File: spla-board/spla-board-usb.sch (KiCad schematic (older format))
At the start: 28 parts, among them J1 USB_B_Micro, U2 FT2232H, U3 93LC66B, X1 FT5HNBPK12.0-T1

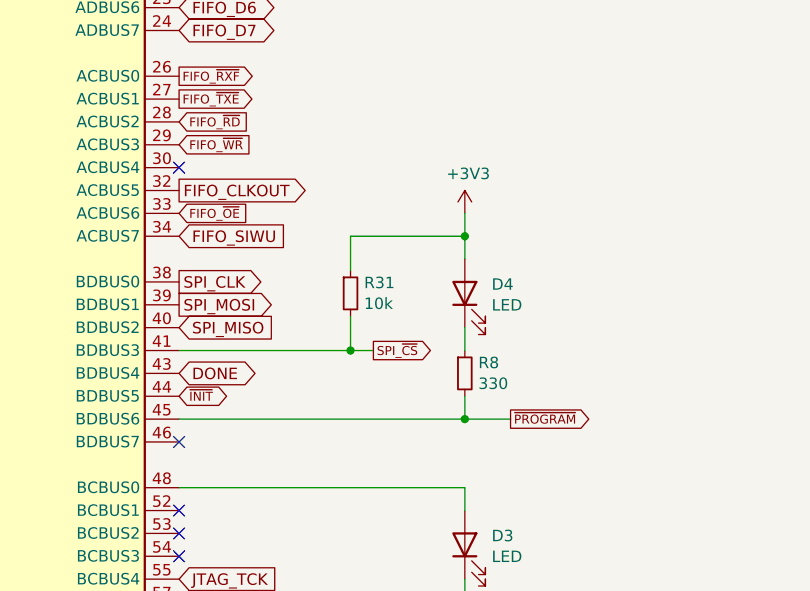
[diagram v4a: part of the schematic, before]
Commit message: schematic/pcb: Pinswap entire FPGA to put LEDs/TPs on south edge.
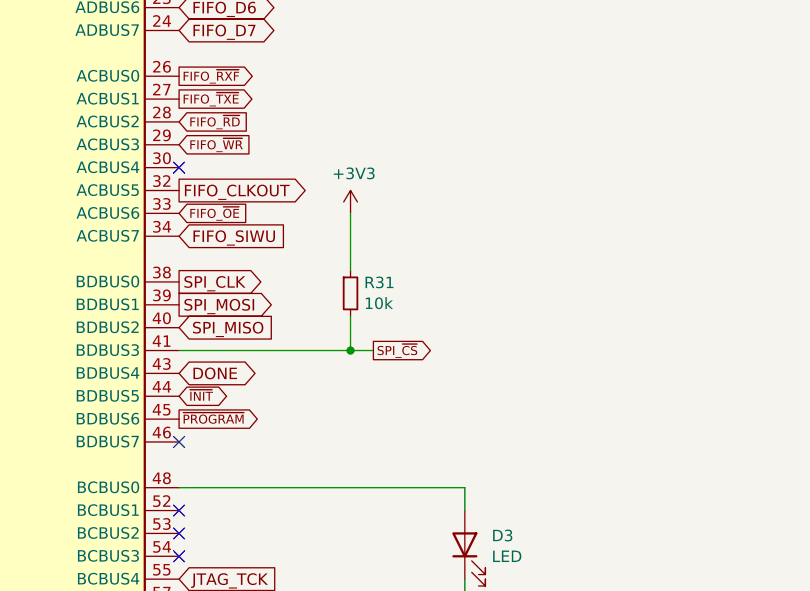
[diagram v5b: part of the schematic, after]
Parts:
- removed D4: LED, LED_SMD:LED_0805_2012Metric, symbol Device:LED
- removed R8: 330, Resistor_SMD:R_0603_1608Metric, symbol Device:R_Small
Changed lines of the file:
@@
 Text GLabel 11150 6050 2    39   BiDi ~ 0
 ~INIT
-Text GLabel 12600 6150 2    39   Output ~ 0
+Text GLabel 11150 6150 2    39   Output ~ 0
 ~PROGRAM
 Text GLabel 11150 5950 2    50   BiDi ~ 0
@@
 $EndComp
 $Comp
-L Device:LED D4
-U 1 1 5E9C89B2
-P 12400 5600
-AR Path="/5E4F712F/5E9C89B2" Ref="D4"  Part="1"
-AR Path="/5E50D39B/5E9C89B2" Ref="D?"  Part="1"
-AR Path="/5E4D8358/5E9C89B2" Ref="D?"  Part="1"
-F 0 "D4" V 12439 5483 50  0000 R CNN
-F 1 "LED" V 12348 5483 50  0000 R CNN
-F 2 "LED_SMD:LED_0805_2012Metric" H 12400 5600 50  0001 C CNN
-F 3 "~" H 12400 5600 50  0001 C CNN
-F 4 "732-4986-1-ND" H 12400 5600 50  0001 C CNN "Digikey"
-F 5 "150080VS75000" H 12400 5600 50  0001 C CNN "Manufacturer Id"
-F 6 "Wuerth Electronik" H 12400 5600 50  0001 C CNN "Manufacturer"
-	1    12400 5600
-	0    -1   -1   0
-$EndComp
-Wire Wire Line
-	12400 5750 12400 5850
-Wire Wire Line
-	12400 6050 12400 6150
-$Comp
 L power:+3V3 #PWR?
 U 1 1 5E9C89C1
-P 12400 5250
+P 11900 5250
 AR Path="/5E4D8358/5E9C89C1" Ref="#PWR?"  Part="1"
 AR Path="/5E4F712F/5E9C89C1" Ref="#PWR053"  Part="1"
-F 0 "#PWR053" H 12400 5100 50  0001 C CNN
-F 1 "+3V3" H 12415 5423 50  0000 C CNN
-F 2 "" H 12400 5250 50  0001 C CNN
-F 3 "" H 12400 5250 50  0001 C CNN
-	1    12400 5250
-	1    0    0    -1
-$EndComp
-Wire Wire Line
-	12400 5250 12400 5350
-Wire Wire Line
-	12600 6150 12400 6150
-Connection ~ 12400 6150
-Wire Wire Line
-	12400 6150 11150 6150
+F 0 "#PWR053" H 11900 5100 50  0001 C CNN
+F 1 "+3V3" H 11915 5423 50  0000 C CNN
+F 2 "" H 11900 5250 50  0001 C CNN
+F 3 "" H 11900 5250 50  0001 C CNN
+	1    11900 5250
+	1    0    0    -1
+$EndComp
 Wire Wire Line
 	6350 7450 7550 7450
@@
 $EndComp
 Wire Wire Line
-	12400 5350 11900 5350
-Wire Wire Line
-	11900 5350 11900 5500
-Connection ~ 12400 5350
-Wire Wire Line
-	12400 5350 12400 5450
-Wire Wire Line
 	2800 4450 2800 4200
 Wire Wire Line
@@
 F 6 "GRM188R61E475KE11D" H 7300 2900 50  0001 C CNN "Manufacturer Id"
 	1    7300 2900
-	1    0    0    -1
-$EndComp
-$Comp
-L Device:R_Small R8
-U 1 1 5E9C89B8
-P 12400 5950
-AR Path="/5E4F712F/5E9C89B8" Ref="R8"  Part="1"
-AR Path="/5E50D39B/5E9C89B8" Ref="R?"  Part="1"
-AR Path="/5E4D8358/5E9C89B8" Ref="R?"  Part="1"
-F 0 "R8" H 12459 5996 50  0000 L CNN
-F 1 "330" H 12459 5905 50  0000 L CNN
-F 2 "Resistor_SMD:R_0603_1608Metric" H 12400 5950 50  0001 C CNN
-F 3 "~" H 12400 5950 50  0001 C CNN
-F 4 "RMCF0603JT330RCT-ND" H 12400 5950 50  0001 C CNN "Digikey"
-F 5 "Stackpole Electronics Inc" H 12400 5950 50  0001 C CNN "Manufacturer"
-F 6 "RMCF0603JT330R" H 12400 5950 50  0001 C CNN "Manufacturer Id"
-	1    12400 5950
 	1    0    0    -1
 $EndComp
@@
 Wire Wire Line
 	3950 3950 3950 4250
+Wire Wire Line
+	11900 5250 11900 5500
 $EndSCHEMATC

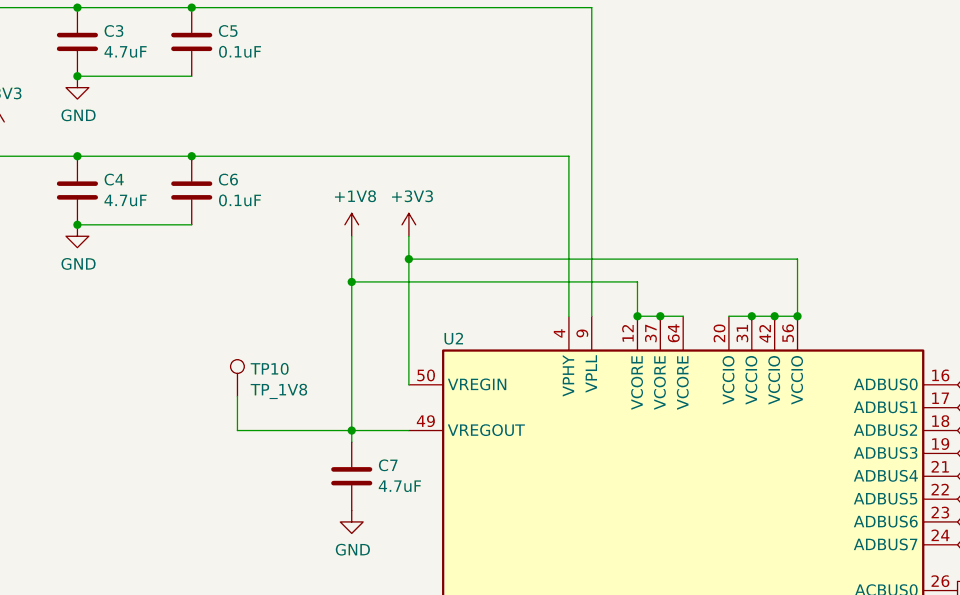
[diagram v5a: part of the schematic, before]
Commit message: schematic/pcb: Add 0-ohm resistor to disconnect FTDI 1.8V regulator.
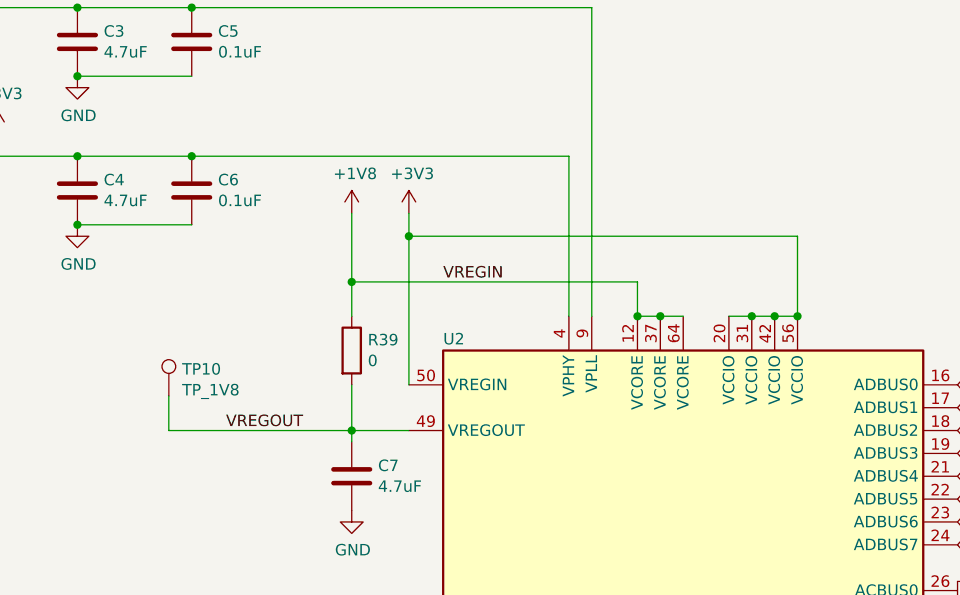
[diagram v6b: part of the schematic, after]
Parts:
- added R39: 0, Resistor_SMD:R_0603_1608Metric, symbol Device:R
- TP10: footprint TestPoint:TestPoint_Pad_D2.0mm -> TestPoint:TestPoint_Pad_D1.0mm
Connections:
- net +1V8: now also R39.1; no longer C7.1, TP10.1, U2.49 (VREGOUT)
- new net VREGOUT: C7.1, R39.2, TP10.1, U2.49 (VREGOUT)
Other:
- moved on the sheet: TP10
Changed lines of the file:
@@
 Weak pullup resistors
 Wire Wire Line
-	10450 3200 10450 3450
+	10450 3100 10450 3450
 Wire Wire Line
 	10150 3450 10250 3450
@@
 Wire Wire Line
 	10350 3450 10450 3450
-Wire Wire Line
-	8500 3300 8500 3950
 Wire Wire Line
 	8500 3950 8750 3950
@@
 L power:+1V8 #PWR0107
 U 1 1 5E5F64FC
-P 8500 3100
-F 0 "#PWR0107" H 8500 2950 50  0001 C CNN
-F 1 "+1V8" H 8515 3273 50  0000 C CNN
-F 2 "" H 8500 3100 50  0001 C CNN
-F 3 "" H 8500 3100 50  0001 C CNN
-	1    8500 3100
-	1    0    0    -1
-$EndComp
-Wire Wire Line
-	8500 3100 8500 3300
-Connection ~ 8500 3300
+P 8500 3000
+F 0 "#PWR0107" H 8500 2850 50  0001 C CNN
+F 1 "+1V8" H 8515 3173 50  0000 C CNN
+F 2 "" H 8500 3000 50  0001 C CNN
+F 3 "" H 8500 3000 50  0001 C CNN
+	1    8500 3000
+	1    0    0    -1
+$EndComp
+Wire Wire Line
+	8500 3000 8500 3300
 $Comp
 L power:GND #PWR0108
@@
 $EndComp
 Wire Wire Line
-	8750 3200 10450 3200
-Wire Wire Line
-	8750 3200 8750 3750
+	8750 3100 10450 3100
+Wire Wire Line
+	8750 3100 8750 3750
 $Comp
 L power:+3V3 #PWR0113
 U 1 1 5E65F7B7
-P 8750 3100
-F 0 "#PWR0113" H 8750 2950 50  0001 C CNN
-F 1 "+3V3" H 8765 3273 50  0000 C CNN
-F 2 "" H 8750 3100 50  0001 C CNN
-F 3 "" H 8750 3100 50  0001 C CNN
-	1    8750 3100
-	1    0    0    -1
-$EndComp
-Connection ~ 8750 3200
-Wire Wire Line
-	8750 3200 8750 3100
+P 8750 3000
+F 0 "#PWR0113" H 8750 2850 50  0001 C CNN
+F 1 "+3V3" H 8765 3173 50  0000 C CNN
+F 2 "" H 8750 3000 50  0001 C CNN
+F 3 "" H 8750 3000 50  0001 C CNN
+	1    8750 3000
+	1    0    0    -1
+$EndComp
+Connection ~ 8750 3100
+Wire Wire Line
+	8750 3100 8750 3000
 Wire Wire Line
 	9450 3450 9450 2750
@@
 L Connector:TestPoint TP10
 U 1 1 5F33FE5B
-P 8000 3800
-F 0 "TP10" H 8058 3918 50  0000 L CNN
-F 1 "TP_1V8" H 8058 3827 50  0000 L CNN
-F 2 "TestPoint:TestPoint_Pad_D2.0mm" H 8200 3800 50  0001 C CNN
-F 3 "~" H 8200 3800 50  0001 C CNN
-	1    8000 3800
-	1    0    0    -1
-$EndComp
-Wire Wire Line
-	8500 3950 8000 3950
-Wire Wire Line
-	8000 3950 8000 3800
+P 7700 3800
+F 0 "TP10" H 7758 3918 50  0000 L CNN
+F 1 "TP_1V8" H 7758 3827 50  0000 L CNN
+F 2 "TestPoint:TestPoint_Pad_D1.0mm" H 7900 3800 50  0001 C CNN
+F 3 "~" H 7900 3800 50  0001 C CNN
+	1    7700 3800
+	1    0    0    -1
+$EndComp
+Wire Wire Line
+	8500 3950 7700 3950
+Wire Wire Line
+	7700 3950 7700 3800
 Text GLabel 8300 8300 2    50   Output ~ 0
 CLK_12MHZ
@@
 Wire Wire Line
 	11900 5250 11900 5500
+$Comp
+L Device:R R39
+U 1 1 5F36220C
+P 8500 3600
+F 0 "R39" H 8570 3646 50  0000 L CNN
+F 1 "0" H 8570 3555 50  0000 L CNN
+F 2 "Resistor_SMD:R_0603_1608Metric" V 8430 3600 50  0001 C CNN
+F 3 "~" H 8500 3600 50  0001 C CNN
+F 4 "2019-RK73Z1JTTDCT-ND" H 8500 3600 50  0001 C CNN "Digikey"
+F 5 "KOA Speer Electronics Inc." H 8500 3600 50  0001 C CNN "Manufacturer"
+F 6 "RK73Z1JTTD" H 8500 3600 50  0001 C CNN "Manufacturer Id"
+	1    8500 3600
+	1    0    0    -1
+$EndComp
+Wire Wire Line
+	8500 3450 8500 3300
+Connection ~ 8500 3300
+Wire Wire Line
+	8500 3750 8500 3950
+Text Label 8900 3300 0    50   ~ 0
+VREGIN
+Text Label 7950 3950 0    50   ~ 0
+VREGOUT
 $EndSCHEMATC

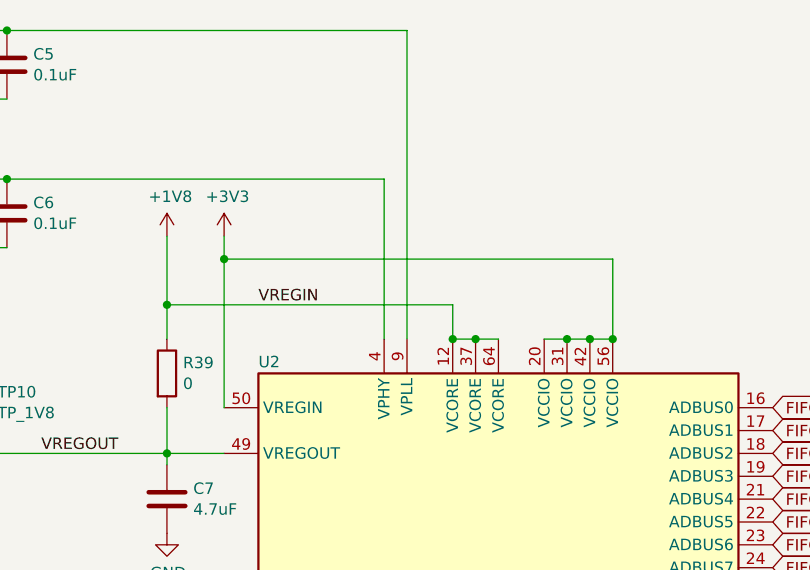
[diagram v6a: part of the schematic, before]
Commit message: pcb/schematic: Rework layout for 0.65mm PPU footprint, as well as other minor issues.
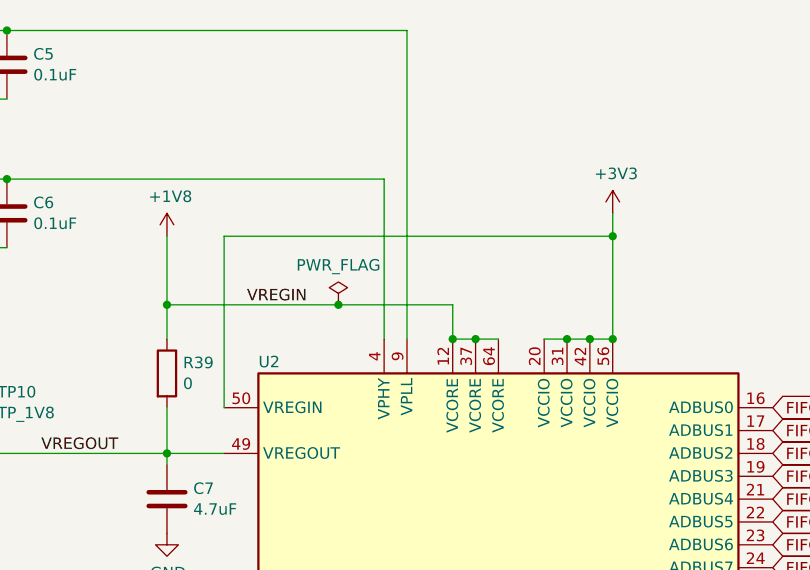
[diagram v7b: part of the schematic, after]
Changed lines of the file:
@@
 Weak pullup resistors
 Wire Wire Line
-	10450 3100 10450 3450
+	10450 3000 10450 3450
 Wire Wire Line
 	10150 3450 10250 3450
@@
 Connection ~ 9750 3450
 Wire Wire Line
-	9750 3300 8500 3300
+	9750 3300 9250 3300
 $Comp
 L power:+3V3 #PWR0109
@@
 $EndComp
 Wire Wire Line
-	8750 3100 10450 3100
-Wire Wire Line
-	8750 3100 8750 3750
+	8750 3000 10450 3000
+Wire Wire Line
+	8750 3000 8750 3750
 $Comp
 L power:+3V3 #PWR0113
 U 1 1 5E65F7B7
-P 8750 3000
-F 0 "#PWR0113" H 8750 2850 50  0001 C CNN
-F 1 "+3V3" H 8765 3173 50  0000 C CNN
-F 2 "" H 8750 3000 50  0001 C CNN
-F 3 "" H 8750 3000 50  0001 C CNN
-	1    8750 3000
-	1    0    0    -1
-$EndComp
-Connection ~ 8750 3100
-Wire Wire Line
-	8750 3100 8750 3000
+P 10450 2900
+F 0 "#PWR0113" H 10450 2750 50  0001 C CNN
+F 1 "+3V3" H 10465 3073 50  0000 C CNN
+F 2 "" H 10450 2900 50  0001 C CNN
+F 3 "" H 10450 2900 50  0001 C CNN
+	1    10450 2900
+	1    0    0    -1
+$EndComp
 Wire Wire Line
 	9450 3450 9450 2750
@@
 Wire Wire Line
 	8500 3750 8500 3950
-Text Label 8900 3300 0    50   ~ 0
+Text Label 8850 3300 0    50   ~ 0
 VREGIN
 Text Label 7950 3950 0    50   ~ 0
 VREGOUT
+$Comp
+L power:PWR_FLAG #FLG0108
+U 1 1 5F75FBCC
+P 9250 3300
+F 0 "#FLG0108" H 9250 3375 50  0001 C CNN
+F 1 "PWR_FLAG" H 9250 3473 50  0000 C CNN
+F 2 "" H 9250 3300 50  0001 C CNN
+F 3 "~" H 9250 3300 50  0001 C CNN
+	1    9250 3300
+	1    0    0    -1
+$EndComp
+Connection ~ 9250 3300
+Wire Wire Line
+	9250 3300 8500 3300
+Wire Wire Line
+	10450 2900 10450 3000
+Connection ~ 10450 3000
 $EndSCHEMATC

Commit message: schematic/pcb: Add 74LVC1G17 buffers for LEDs; arrange layout to suit.
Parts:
- TP10: Digikey (none) -> N/A; Manufacturer (none) -> N/A; Manufacturer Id (none) -> N/A
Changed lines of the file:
@@
 F 2 "TestPoint:TestPoint_Pad_D1.0mm" H 7900 3800 50  0001 C CNN
 F 3 "~" H 7900 3800 50  0001 C CNN
+F 4 "N/A" H 7700 3800 50  0001 C CNN "Digikey"
+F 5 "N/A" H 7700 3800 50  0001 C CNN "Manufacturer"
+F 6 "N/A" H 7700 3800 50  0001 C CNN "Manufacturer Id"
 	1    7700 3800
 	1    0    0    -1
